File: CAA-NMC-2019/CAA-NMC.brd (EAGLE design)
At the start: 33.3 x 100 mm, 41 parts, among them IC1 ATTINY85-20SU, J1 M20-9980346

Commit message: cleanup con't
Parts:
- moved LED1 123.0 mm to (-41.7, 62.5)
- moved LED2 121.6 mm to (-33.3, 62.5)
- moved LED3 120.2 mm to (-25.0, 62.5)
- moved R3 97.2 mm to (-53.3, 6.66)
- moved R4 97.2 mm to (-50.0, 6.66)
- moved C3 91.5 mm to (-50.8, 12.5)
- moved C1 90.1 mm to (-61.7, 16.7)
- moved C2 87.9 mm to (-58.3, 12.5)
- moved U$1 4.17 mm to (0.00, 29.2)

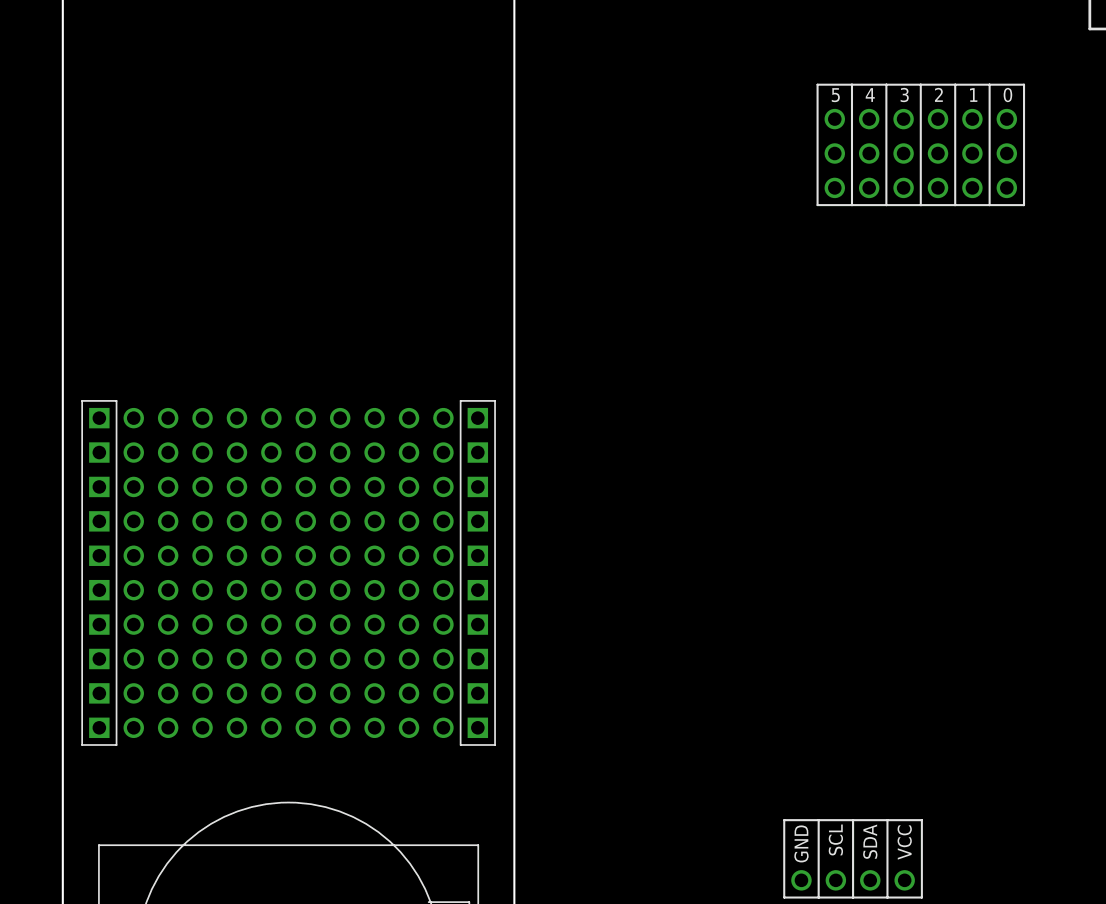
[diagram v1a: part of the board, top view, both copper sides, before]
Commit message: added PB B/Os to proto grid
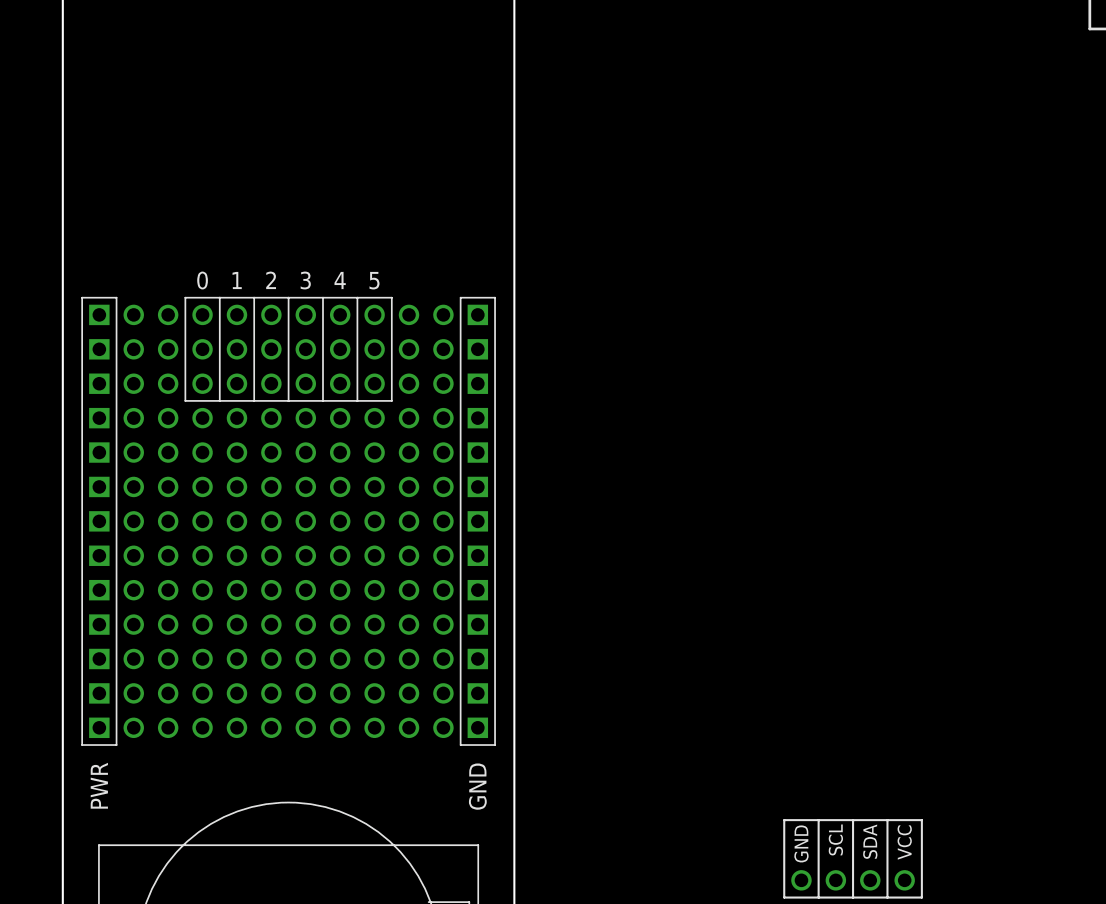
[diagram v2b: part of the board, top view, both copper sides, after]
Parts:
- removed U$75, U$76, U$77, U$78, U$79, U$80, U$81, U$82, U$83, U$84, U$85, U$86, U$87, U$88, U$89, U$90, U$91, U$92: ONE_PAD, BadgeParts:1X01
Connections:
- net GND: now also U$1.GND0, U$1.GND1, U$1.GND2, U$1.GND3, U$1.GND4, U$1.GND5, U$1.GND6, U$1.GND7, U$1.GND8, U$1.GND9
- net PB0: now also U$1.0A, U$1.0B, U$1.0C; no longer U$75.P$1, U$76.P$1, U$77.P$1
- net PB1: now also U$1.1A, U$1.1B, U$1.1C; no longer U$78.P$1, U$79.P$1, U$80.P$1
- net PB2: now also U$1.2A, U$1.2B, U$1.2C; no longer U$81.P$1, U$82.P$1, U$83.P$1
- net PB3: now also U$1.3A, U$1.3B, U$1.3C; no longer U$84.P$1, U$85.P$1, U$86.P$1
- net PB4: now also U$1.4A, U$1.4B, U$1.4C; no longer U$87.P$1, U$88.P$1, U$89.P$1
- net PB5: now also U$1.5A, U$1.5B, U$1.5C; no longer U$90.P$1, U$91.P$1, U$92.P$1
- net VCC: now also U$1.PWR0, U$1.PWR1, U$1.PWR2, U$1.PWR3, U$1.PWR4, U$1.PWR5, U$1.PWR6, U$1.PWR7, U$1.PWR8, U$1.PWR9
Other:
- board text removed: "0"
- board text removed: "1"
- board text removed: "2"
- board text removed: "3"
- board text removed: "4"
- board text removed: "5"

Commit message: custom RGB LED def includes .1uf cap in layout
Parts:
- added D1, D2, D3: WS2812B, BadgeParts:WS2812B
- added R1: 470, SparkFun-Resistors:0603
- added R2: 10k, SparkFun-Resistors:0603
- moved POWER 144.5 mm to (-27.9, 87.9)
- moved U$126 142.9 mm to (-25.6, 89.0)
- moved HELLO 118.9 mm to (-26.9, 78.4)
- moved U$127 118.9 mm to (-30.7, 76.5)
- moved J1 56.2 mm to (-11.1, 92.9)
- moved U$145 54.2 mm to (9.49, 82.6)
- moved C2 41.0 mm to (-28.0, 40.0)
- moved C1 37.8 mm to (-32.0, 40.0)
- moved R4 31.7 mm to (-31.0, 32.0)
- moved R3 31.3 mm to (-35.0, 32.0)
- moved LED3 27.7 mm to (-38.0, 38.0)
- moved C3 22.8 mm to (-39.0, 32.0)
- moved LED1 16.9 mm to (-38.0, 46.0)
- moved IC1 16.7 mm to (10.2, 95.7)
- moved U$123 16.7 mm to (8.90, 90.6)
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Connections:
- new net N$3: D1.DO, D2.DI
- new net N$4: D2.DO, D3.DI
- new net N$5: D1.DI, R1.1
- net GND: now also D1.CAP1, D1.GND, D2.CAP1, D2.GND, D3.CAP1, D3.GND, U$2.GND
- net PB4: now also R1.2, R2.1
- net VCC: now also D1.CAP2, D1.VCC, D2.CAP2, D2.VCC, D3.CAP2, D3.VCC, R2.2, U$2.VCC

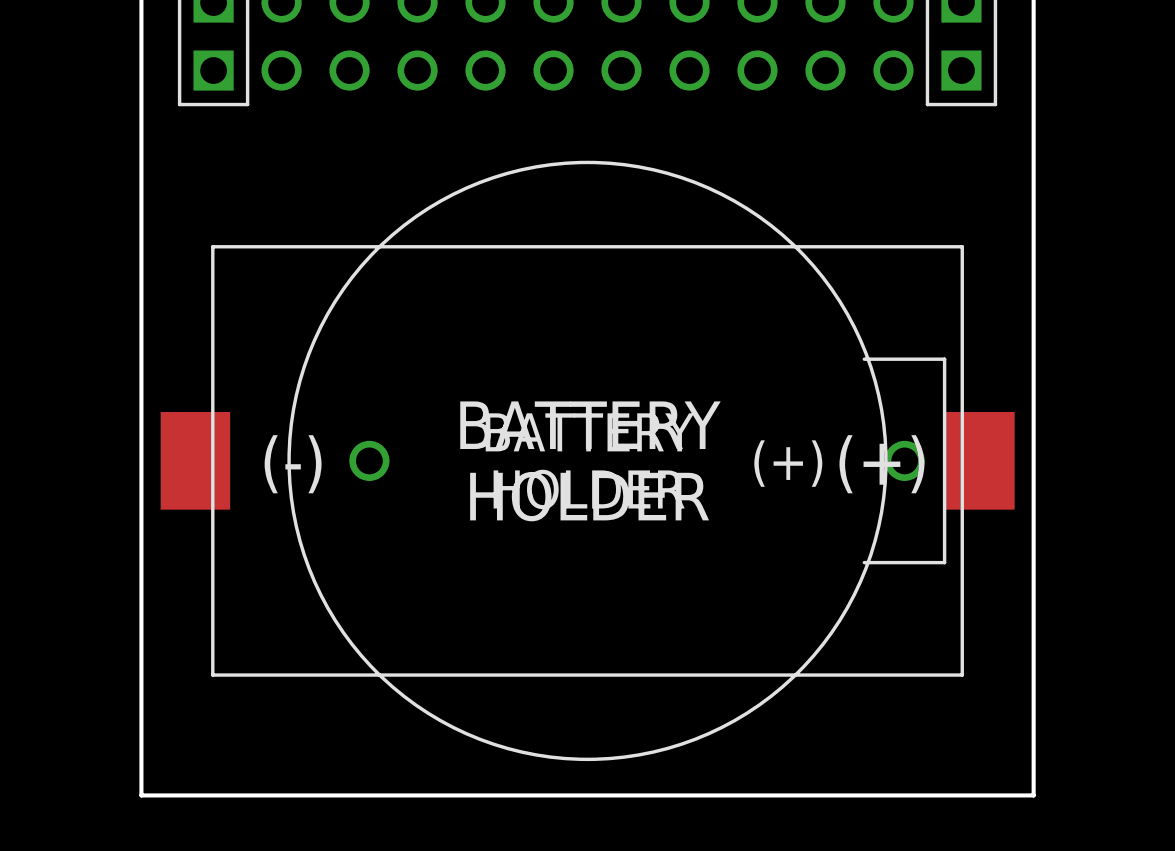
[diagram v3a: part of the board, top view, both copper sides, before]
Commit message: fixed battery orientation
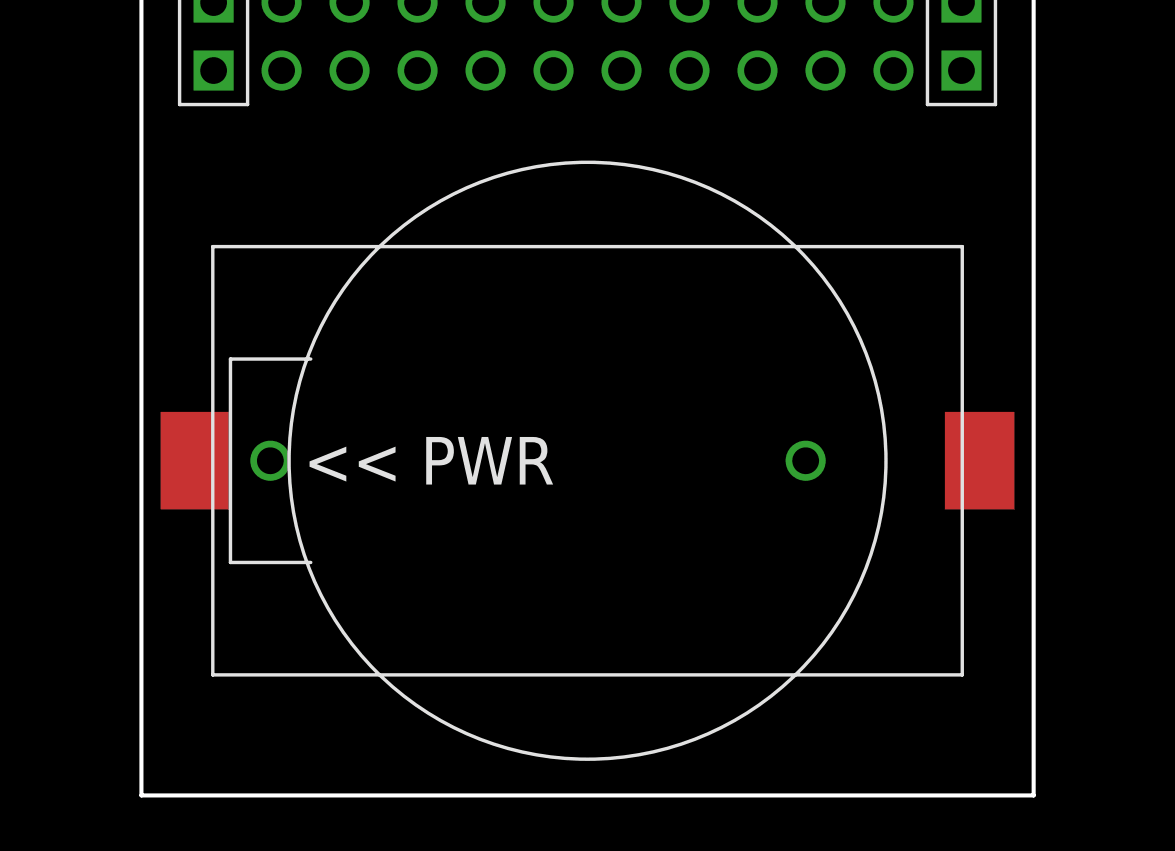
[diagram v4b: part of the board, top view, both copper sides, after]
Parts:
- removed U$144: SMT-BATTERY-HOLDER, BadgeParts:SMT-CR-HOLDER
- added U$3: THRU-CR-HOLDER, BadgeParts:THRU-CR-HOLDER
- U$2: value THRU-CR-HOLDER -> SMT-BATTERY-HOLDER; device BadgeParts:THRU-CR-HOLDER -> BadgeParts:SMT-CR-HOLDER
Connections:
- new net VBAT: U$145.4
- new net VUSB: U$145.6
- net GND: no longer U$144.GND, U$2.GND
- net VCC: now also U$145.5; no longer U$144.VCC, U$2.VCC
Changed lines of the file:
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@@
 <element name="U$126" library="BadgeParts" package="AXIAL-0.3" value="RESISTOR" x="-25.576" y="89.037" smashed="yes" rot="R270"/>
 <element name="U$127" library="BadgeParts" package="AXIAL-0.3" value="RESISTOR" x="-30.709" y="76.539" smashed="yes" rot="R270"/>
-<element name="U$144" library="BadgeParts" package="SMT-CR-HOLDER" value="SMT-BATTERY-HOLDER" x="0" y="12.498" smashed="yes" rot="R180"/>
 <element name="U$145" library="BadgeParts" package="SMT-SWITCH" value="SMT-SWITCH" x="9.48895" y="82.552378125" smashed="yes"/>
 <element name="U$1" library="BadgeParts" package="PROTO" value="PROTO" x="0" y="27.082" smashed="yes"/>
-<element name="U$2" library="BadgeParts" package="THRU-CR-HOLDER" value="THRU-CR-HOLDER" x="0" y="12.498" smashed="yes"/>
 <element name="LED1" library="SparkFun-LED" library_urn="urn:adsk.eagle:library:529" package="WS2812B" package3d_urn="urn:adsk.eagle:package:39369/1" value="WS2812B" x="-38" y="46" smashed="yes">
 <attribute name="NAME" x="-38" y="48.794" size="0.6096" layer="25" font="vector" ratio="20" align="bottom-center"/>
@@
 <attribute name="VALUE" x="5.21" y="68.01" size="0.6096" layer="27" font="vector" ratio="20" align="top-center"/>
 </element>
+<element name="U$2" library="BadgeParts" package="SMT-CR-HOLDER" value="SMT-BATTERY-HOLDER" x="0" y="12.504" smashed="yes"/>
+<element name="U$3" library="BadgeParts" package="THRU-CR-HOLDER" value="THRU-CR-HOLDER" x="0" y="12.504" smashed="yes"/>
 </elements>
 <signals>
@@
 <contactref element="U$123" pad="P$2"/>
 <contactref element="U$126" pad="P$4"/>
-<contactref element="U$144" pad="VCC"/>
 <contactref element="U$1" pad="PWR8"/>
 <contactref element="U$1" pad="PWR4"/>
@@
 <contactref element="U$1" pad="PWR7"/>
 <contactref element="U$1" pad="PWR3"/>
-<contactref element="U$2" pad="VCC"/>
 <contactref element="D1" pad="VCC"/>
 <contactref element="D1" pad="CAP2"/>
@@
 <contactref element="D3" pad="CAP2"/>
 <contactref element="R2" pad="2"/>
+<contactref element="U$145" pad="5"/>
 <wire x1="11.436" y1="90.64" x2="13.916" y2="97.5869" width="0" layer="19" extent="1-1"/>
-<wire x1="-8.542059375" y1="94.195115625" x2="11.436" y2="90.64" width="0" layer="19" extent="1-1"/>
-<wire x1="-25.576" y1="85.227" x2="-8.542059375" y2="94.195115625" width="0" layer="19" extent="1-1"/>
-<wire x1="-13.97" y1="49.942" x2="-25.576" y2="85.227" width="0" layer="19" extent="1-1"/>
+<wire x1="9.48895" y1="85.302378125" x2="11.436" y2="90.64" width="0" layer="19" extent="1-1"/>
+<wire x1="11.32" y1="68.573" x2="9.48895" y2="85.302378125" width="0" layer="19" extent="1-1"/>
+<wire x1="6.06" y1="68.772" x2="11.32" y2="68.573" width="0" layer="19" extent="1-1"/>
+<wire x1="0.895" y1="68.573" x2="6.06" y2="68.772" width="0" layer="19" extent="1-1"/>
+<wire x1="12.997" y1="62.973" x2="11.32" y2="68.573" width="0" layer="19" extent="1-1"/>
+<wire x1="2.572" y1="62.973" x2="0.895" y2="68.573" width="0" layer="19" extent="1-1"/>
+<wire x1="-7.838" y1="62.973" x2="0.895" y2="68.573" width="0" layer="19" extent="1-1"/>
+<wire x1="-9.515" y1="68.573" x2="-7.838" y2="62.973" width="0" layer="19" extent="1-1"/>
+<wire x1="-13.97" y1="49.942" x2="-7.838" y2="62.973" width="0" layer="19" extent="1-1"/>
 <wire x1="-13.97" y1="47.402" x2="-13.97" y2="49.942" width="0" layer="19" extent="1-1"/>
 <wire x1="-13.97" y1="44.862" x2="-13.97" y2="47.402" width="0" layer="19" extent="1-1"/>
@@
 <wire x1="-13.97" y1="29.622" x2="-13.97" y2="32.162" width="0" layer="19" extent="1-1"/>
 <wire x1="-13.97" y1="27.082" x2="-13.97" y2="29.622" width="0" layer="19" extent="1-1"/>
-<wire x1="11.85" y1="12.498" x2="-13.97" y2="27.082" width="0" layer="19" extent="1-1"/>
-<wire x1="14.65" y1="12.498" x2="11.85" y2="12.498" width="0" layer="19" extent="1-1"/>
-<wire x1="45.48" y1="17.905" x2="14.65" y2="12.498" width="0" layer="19" extent="1-1"/>
-<wire x1="0.895" y1="68.573" x2="11.85" y2="12.498" width="0" layer="19" extent="1-1"/>
-<wire x1="2.572" y1="62.973" x2="0.895" y2="68.573" width="0" layer="19" extent="1-1"/>
-<wire x1="-7.838" y1="62.973" x2="2.572" y2="62.973" width="0" layer="19" extent="1-1"/>
-<wire x1="11.32" y1="68.573" x2="-7.838" y2="62.973" width="0" layer="19" extent="1-1"/>
-<wire x1="12.997" y1="62.973" x2="11.32" y2="68.573" width="0" layer="19" extent="1-1"/>
-<wire x1="6.06" y1="68.772" x2="12.997" y2="62.973" width="0" layer="19" extent="1-1"/>
-<wire x1="-9.515" y1="68.573" x2="-7.838" y2="62.973" width="0" layer="19" extent="1-1"/>
+<wire x1="-8.542059375" y1="94.195115625" x2="9.48895" y2="85.302378125" width="0" layer="19" extent="1-1"/>
+<wire x1="-25.576" y1="85.227" x2="-8.542059375" y2="94.195115625" width="0" layer="19" extent="1-1"/>
+<wire x1="45.48" y1="17.905" x2="12.997" y2="62.973" width="0" layer="19" extent="1-1"/>
 </signal>
 <signal name="PB3">
@@
 <contactref element="U$71" pad="P$1"/>
 <contactref element="U$123" pad="P$1"/>
-<contactref element="U$144" pad="GND"/>
 <contactref element="U$1" pad="GND3"/>
 <contactref element="U$1" pad="GND8"/>
@@
 <contactref element="U$1" pad="GND7"/>
 <contactref element="U$1" pad="GND9"/>
-<contactref element="U$2" pad="GND"/>
 <contactref element="LED3" pad="3"/>
 <contactref element="C3" pad="2"/>
@@
 <wire x1="-27.94" y1="86.637" x2="-13.622059375" y2="94.195115625" width="0" layer="19" extent="1-1"/>
 <wire x1="-26.899" y1="77.174" x2="-27.94" y2="86.637" width="0" layer="19" extent="1-1"/>
-<wire x1="13.97" y1="49.942" x2="8.896" y2="90.64" width="0" layer="19" extent="1-1"/>
+<wire x1="-12.992" y1="66.173" x2="-26.899" y2="77.174" width="0" layer="19" extent="1-1"/>
+<wire x1="-11.315" y1="68.573" x2="-12.992" y2="66.173" width="0" layer="19" extent="1-1"/>
+<wire x1="-2.582" y1="66.173" x2="-11.315" y2="68.573" width="0" layer="19" extent="1-1"/>
+<wire x1="-0.905" y1="68.573" x2="-2.582" y2="66.173" width="0" layer="19" extent="1-1"/>
+<wire x1="7.843" y1="66.173" x2="-0.905" y2="68.573" width="0" layer="19" extent="1-1"/>
+<wire x1="9.52" y1="68.573" x2="7.843" y2="66.173" width="0" layer="19" extent="1-1"/>
+<wire x1="13.97" y1="49.942" x2="7.843" y2="66.173" width="0" layer="19" extent="1-1"/>
 <wire x1="13.97" y1="47.402" x2="13.97" y2="49.942" width="0" layer="19" extent="1-1"/>
 <wire x1="13.97" y1="44.862" x2="13.97" y2="47.402" width="0" layer="19" extent="1-1"/>
@@
 <wire x1="13.97" y1="27.082" x2="13.97" y2="29.622" width="0" layer="19" extent="1-1"/>
 <wire x1="37.86" y1="17.905" x2="13.97" y2="27.082" width="0" layer="19" extent="1-1"/>
-<wire x1="-8.15" y1="12.498" x2="13.97" y2="27.082" width="0" layer="19" extent="1-1"/>
-<wire x1="-14.65" y1="12.498" x2="-8.15" y2="12.498" width="0" layer="19" extent="1-1"/>
-<wire x1="-33.577" y1="47.6" x2="-14.65" y2="12.498" width="0" layer="19" extent="1-1"/>
+<wire x1="-33.577" y1="47.6" x2="-12.992" y2="66.173" width="0" layer="19" extent="1-1"/>
 <wire x1="-40.577" y1="47.6" x2="-33.577" y2="47.6" width="0" layer="19" extent="1-1"/>
 <wire x1="-31.15" y1="40" x2="-33.577" y2="47.6" width="0" layer="19" extent="1-1"/>
@@
 <wire x1="-40.577" y1="39.6" x2="-40.577" y2="47.6" width="0" layer="19" extent="1-1"/>
 <wire x1="-38.15" y1="32" x2="-40.577" y2="39.6" width="0" layer="19" extent="1-1"/>
-<wire x1="-11.315" y1="68.573" x2="-38.15" y2="32" width="0" layer="19" extent="1-1"/>
-<wire x1="-12.992" y1="66.173" x2="-11.315" y2="68.573" width="0" layer="19" extent="1-1"/>
-<wire x1="-2.582" y1="66.173" x2="-11.315" y2="68.573" width="0" layer="19" extent="1-1"/>
-<wire x1="-0.905" y1="68.573" x2="-2.582" y2="66.173" width="0" layer="19" extent="1-1"/>
-<wire x1="9.52" y1="68.573" x2="-12.992" y2="66.173" width="0" layer="19" extent="1-1"/>
-<wire x1="7.843" y1="66.173" x2="9.52" y2="68.573" width="0" layer="19" extent="1-1"/>
 </signal>
 <signal name="PB2">
@@
 <wire x1="-6.06" y1="68.772" x2="-12.992" y2="62.973" width="0" layer="19" extent="1-1"/>
 </signal>
+<signal name="VBAT">
+<contactref element="U$145" pad="4"/>
+</signal>
+<signal name="VUSB">
+<contactref element="U$145" pad="6"/>
+</signal>
 </signals>
